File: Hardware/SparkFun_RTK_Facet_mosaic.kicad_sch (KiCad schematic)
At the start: 28 parts, among them J3 Qwiic_RA, J5 Conn_01x12_FPC_0.5mm, J6 Conn_01x12_FPC_0.5mm, J7 Conn_01x12_FPC_0.5mm, U1 ESP32-WROVER-E-N16R8

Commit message: Routed
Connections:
- net SD_CLK: now also D2.5 (K4); no longer D2.4 (K3)
- net SD_CMD: now also D2.4 (K3); no longer D2.5 (K4)
- net SD_DATA: now also D2.1 (K1); no longer D2.3 (K2)
- net at J7.5 (Pin_5), R28.2: now also D2.3 (K2); no longer D2.1 (K1)
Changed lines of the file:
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@@
   (junction (at 148.59 49.53) (diameter 0) (color 0 0 0 0)
   )
-  (junction (at 130.81 52.07) (diameter 0) (color 0 0 0 0)
-  )
-  (junction (at 125.73 46.99) (diameter 0) (color 0 0 0 0)
+  (junction (at 133.35 52.07) (diameter 0) (color 0 0 0 0)
   )
   (junction (at 34.29 62.23) (diameter 0) (color 0 0 0 0)
@@
   (junction (at 34.29 36.83) (diameter 0) (color 0 0 0 0)
   )
+  (junction (at 125.73 54.61) (diameter 0) (color 0 0 0 0)
+  )
   (junction (at 34.29 39.37) (diameter 0) (color 0 0 0 0)
   )
   (junction (at 59.69 144.78) (diameter 0) (color 0 0 0 0)
   )
-  (junction (at 128.27 54.61) (diameter 0) (color 0 0 0 0)
-  )
   (junction (at 38.1 49.53) (diameter 0) (color 0 0 0 0)
   )
@@
   (junction (at 58.42 109.22) (diameter 0) (color 0 0 0 0)
   )
+  (junction (at 128.27 46.99) (diameter 0) (color 0 0 0 0)
+  )
   (junction (at 55.88 64.77) (diameter 0) (color 0 0 0 0)
   )
-  (junction (at 133.35 49.53) (diameter 0) (color 0 0 0 0)
+  (junction (at 130.81 49.53) (diameter 0) (color 0 0 0 0)
   )
   (wire (pts (xy 97.79 110.49) (xy 99.06 110.49))
@@
     (stroke (width 0) (type default))
   )
+  (wire (pts (xy 130.81 49.53) (xy 148.59 49.53))
+    (stroke (width 0) (type default))
+  )
   (wire (pts (xy 222.25 81.28) (xy 222.25 82.55))
     (stroke (width 0) (type default))
@@
     (stroke (width 0) (type default))
   )
+  (wire (pts (xy 133.35 52.07) (xy 133.35 64.77))
+    (stroke (width 0) (type default))
+  )
   (wire (pts (xy 212.09 50.8) (xy 212.09 52.07))
     (stroke (width 0) (type default))
@@
     (stroke (width 0) (type default))
   )
-  (wire (pts (xy 130.81 52.07) (xy 130.81 64.77))
-    (stroke (width 0) (type default))
-  )
   (wire (pts (xy 111.76 57.15) (xy 135.89 57.15))
     (stroke (width 0) (type default))
   )
-  (wire (pts (xy 125.73 46.99) (xy 125.73 64.77))
-    (stroke (width 0) (type default))
-  )
   (wire (pts (xy 54.61 54.61) (xy 55.88 54.61))
     (stroke (width 0) (type default))
@@
     (stroke (width 0) (type default))
   )
-  (wire (pts (xy 111.76 46.99) (xy 125.73 46.99))
+  (wire (pts (xy 128.27 46.99) (xy 128.27 64.77))
     (stroke (width 0) (type default))
   )
@@
     (stroke (width 0) (type default))
   )
+  (wire (pts (xy 125.73 54.61) (xy 156.21 54.61))
+    (stroke (width 0) (type default))
+  )
+  (wire (pts (xy 133.35 52.07) (xy 157.48 52.07))
+    (stroke (width 0) (type default))
+  )
   (wire (pts (xy 33.02 62.23) (xy 34.29 62.23))
     (stroke (width 0) (type default))
@@
     (stroke (width 0) (type default))
   )
-  (wire (pts (xy 128.27 54.61) (xy 128.27 64.77))
-    (stroke (width 0) (type default))
-  )
   (wire (pts (xy 97.79 151.13) (xy 99.06 151.13))
     (stroke (width 0) (type default))
@@
     (stroke (width 0) (type default))
   )
+  (wire (pts (xy 128.27 46.99) (xy 140.97 46.99))
+    (stroke (width 0) (type default))
+  )
   (wire (pts (xy 54.61 46.99) (xy 55.88 46.99))
     (stroke (width 0) (type default))
@@
     (stroke (width 0) (type default))
   )
-  (wire (pts (xy 133.35 49.53) (xy 133.35 64.77))
-    (stroke (width 0) (type default))
-  )
   (wire (pts (xy 97.79 107.95) (xy 99.06 107.95))
     (stroke (width 0) (type default))
@@
     (stroke (width 0) (type default))
   )
+  (wire (pts (xy 130.81 49.53) (xy 130.81 64.77))
+    (stroke (width 0) (type default))
+  )
   (wire (pts (xy 38.1 49.53) (xy 38.1 48.26))
     (stroke (width 0) (type default))
@@
     (stroke (width 0) (type default))
   )
-  (wire (pts (xy 111.76 49.53) (xy 133.35 49.53))
-    (stroke (width 0) (type default))
-  )
   (wire (pts (xy 33.02 36.83) (xy 34.29 36.83))
     (stroke (width 0) (type default))
@@
     (stroke (width 0) (type default))
   )
-  (wire (pts (xy 130.81 52.07) (xy 157.48 52.07))
+  (wire (pts (xy 111.76 52.07) (xy 133.35 52.07))
     (stroke (width 0) (type default))
   )
@@
     (stroke (width 0) (type default))
   )
+  (wire (pts (xy 125.73 54.61) (xy 125.73 64.77))
+    (stroke (width 0) (type default))
+  )
   (wire (pts (xy 59.69 172.72) (xy 59.69 171.45))
     (stroke (width 0) (type default))
   )
-  (wire (pts (xy 125.73 46.99) (xy 140.97 46.99))
-    (stroke (width 0) (type default))
-  )
-  (wire (pts (xy 111.76 52.07) (xy 130.81 52.07))
+  (wire (pts (xy 111.76 46.99) (xy 128.27 46.99))
     (stroke (width 0) (type default))
   )
@@
     (stroke (width 0) (type default))
   )
-  (wire (pts (xy 128.27 54.61) (xy 156.21 54.61))
+  (wire (pts (xy 111.76 54.61) (xy 125.73 54.61))
     (stroke (width 0) (type default))
   )
@@
     (stroke (width 0) (type default))
   )
-  (wire (pts (xy 133.35 49.53) (xy 148.59 49.53))
+  (wire (pts (xy 111.76 49.53) (xy 130.81 49.53))
     (stroke (width 0) (type default))
   )
@@
     (stroke (width 0) (type default))
   )
-  (wire (pts (xy 111.76 54.61) (xy 128.27 54.61))
-    (stroke (width 0) (type default))
-  )

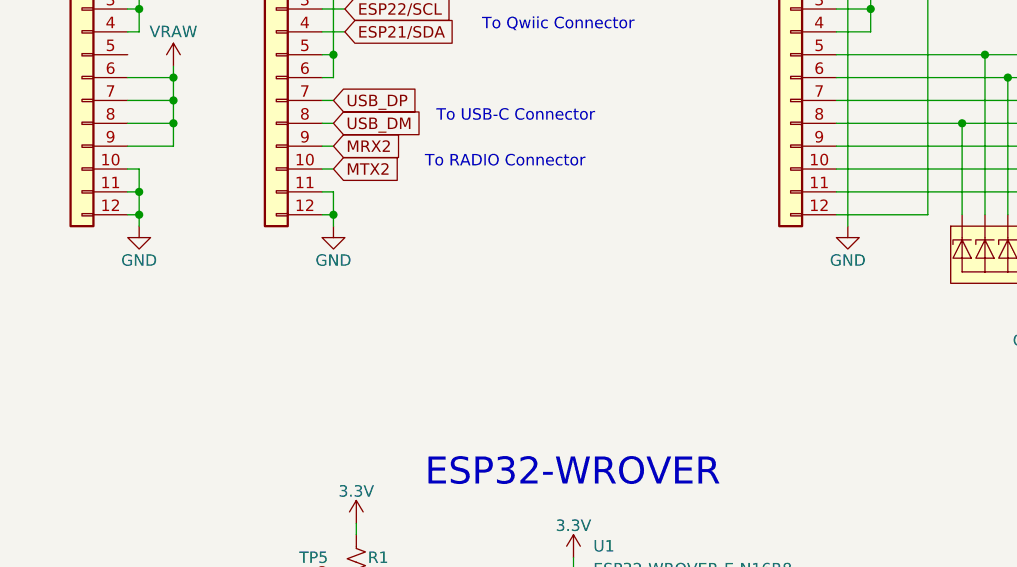
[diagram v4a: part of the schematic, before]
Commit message: Add missing PROD_IDs
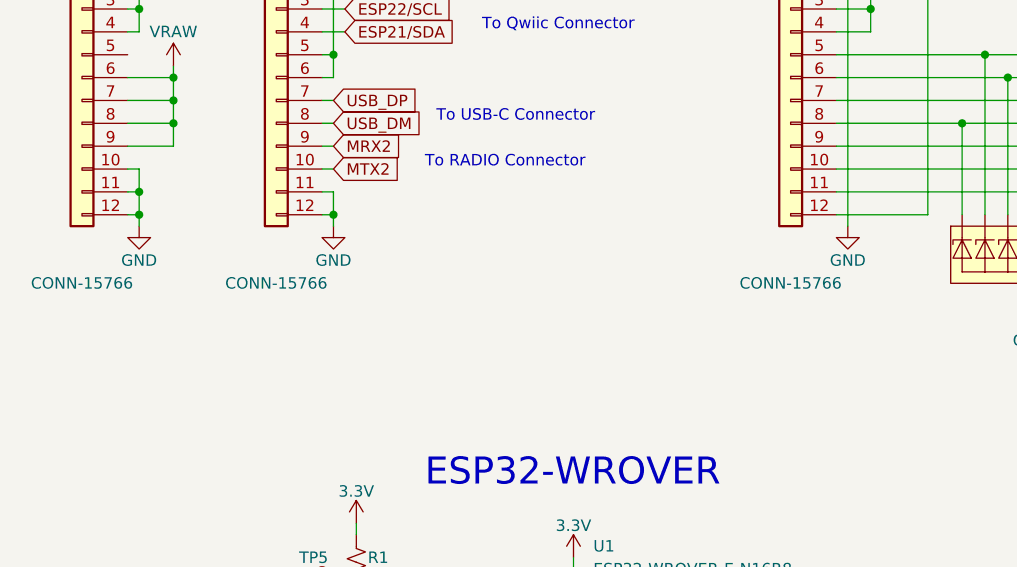
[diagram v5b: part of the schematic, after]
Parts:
- J5, J6, J7: PROD_ID (none) -> CONN-15766
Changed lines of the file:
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@@
       (effects (font (size 1.27 1.27)) hide)
+    )
+    (property "PROD_ID" "CONN-15766" (at 27.94 72.39 0)
+      (effects (font (size 1.27 1.27)))
     )
     (pin "1")
@@
       (effects (font (size 1.27 1.27)) hide)
     )
+    (property "PROD_ID" "CONN-15766" (at 49.53 72.39 0)
+      (effects (font (size 1.27 1.27)))
+    )
     (pin "1")
     (pin "10")
@@
       (effects (font (size 1.27 1.27)) hide)
     )
-    (pin "1")
+    (property "PROD_ID" "CONN-15766" (at 106.68 72.39 0)
+      (effects (font (size 1.27 1.27)))
+    )
+    (pin "1")

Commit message: Add missing PROD_ID
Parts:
- U1: PROD_ID IC- -> IC-21314
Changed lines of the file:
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@@
       (effects (font (size 1.27 1.27)) hide)
     )
-    (property "PROD_ID" "IC-" (at 81.28 195.58 0)
+    (property "PROD_ID" "IC-21314" (at 81.28 195.58 0)
       (effects (font (size 1.27 1.27)) hide)
     )

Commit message: v1.1 routed
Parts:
- J3: footprint SparkFun-Connector:JST04_1MM_RA -> SparkFun-Connector:JST_SMD_1.0mm-4_RA
- J5, J6, J7: footprint SparkFun-Connector:FPC_12_0.5MM -> SparkFun-Connector:FPC_0.5mm-12
- JP1: footprint SparkFun-Jumper:SMT-JUMPER_3_2-NC_TRACE_SILK -> SparkFun-Jumper:Jumper_3_NC-2_Trace
- TP13, TP5: footprint SparkFun-Connector:1X01 -> SparkFun-Connector:1x01
- U7: footprint SparkFun-Aesthetic:ORDERING_INSTRUCTIONS -> SparkFun-Aesthetic:Ordering_Instructions
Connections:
- net ESP12/MUXB: now reaches U1.14 (IOA12)
- net ESP2/MUXA: now reaches U1.24 (IOA2)
- net ESP18/MUXA: no longer names the net of U1.30 (IO18)
- net ESP19/MUXB renamed ESP19/CHG_LED2
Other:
- note added: "Connectors"
- moved on the sheet: C1, C2, C3, J3, JP1, R1, R3, R4, R7, R8, TP5, U1
